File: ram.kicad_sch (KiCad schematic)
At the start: 7 parts, among them U1 LFE5U-25F-6BG381C, U2 MT48LC16M16A2TG

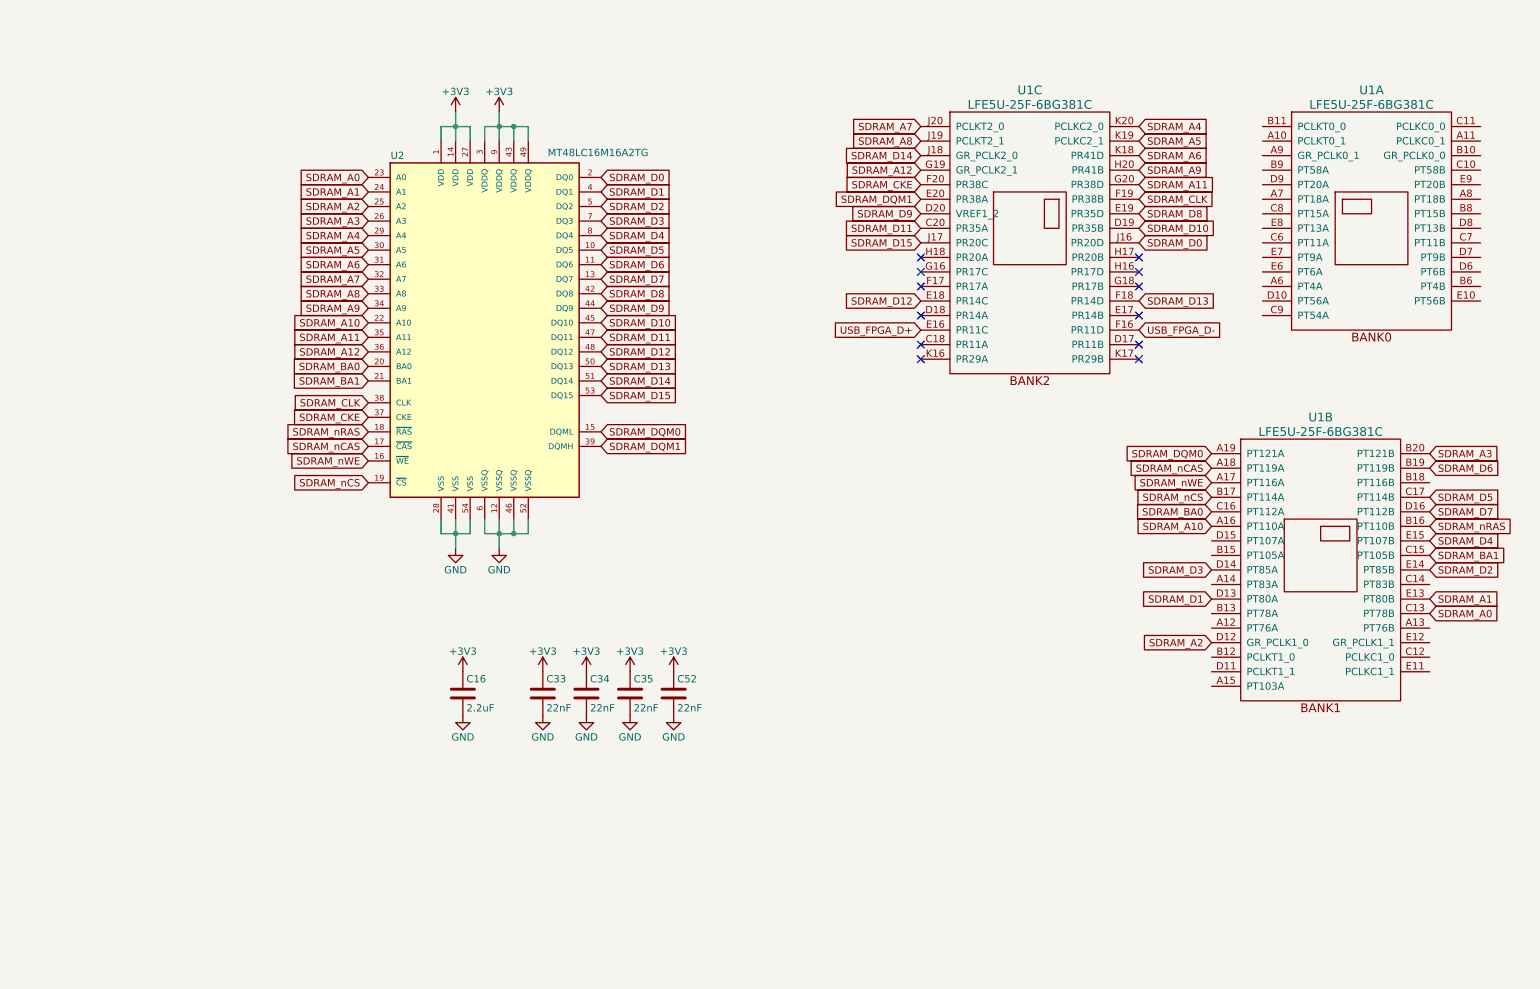
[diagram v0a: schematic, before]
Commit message: Routed Level Shifters + Flash
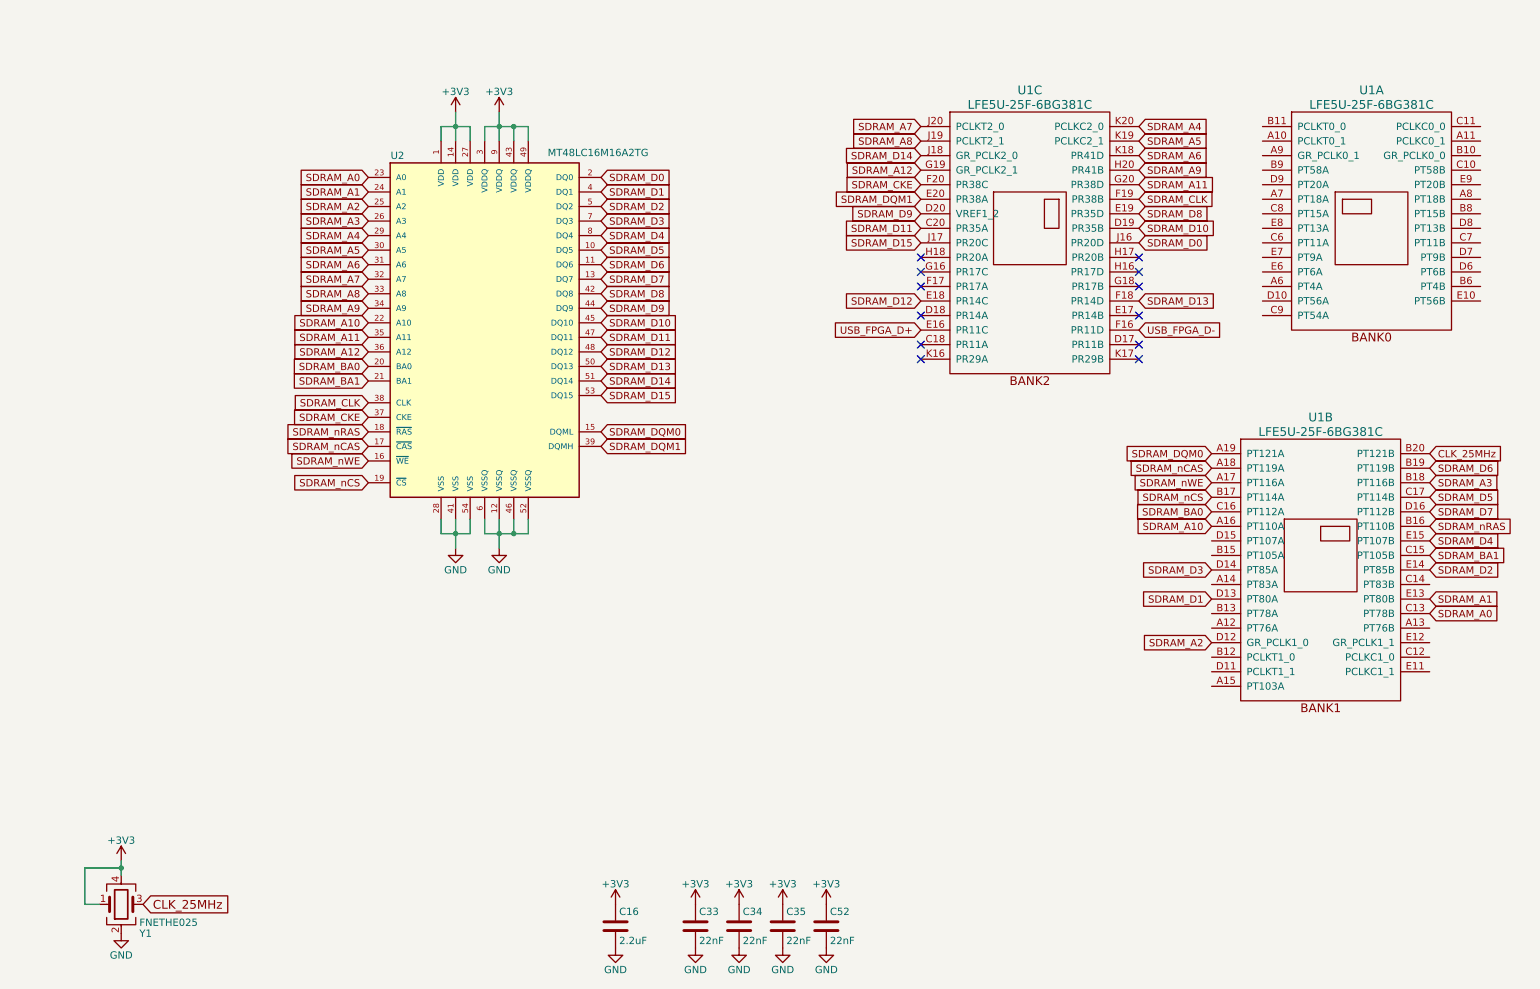
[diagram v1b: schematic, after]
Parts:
- added Y1: FNETHE025, oscxo:Crystal_SMD_7050_4Pads, symbol Device:Crystal_GND24
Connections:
- net +3V3: now also Y1.1, Y1.4
- net GND: now also Y1.2
- net SDRAM_A3: now also U1.B18 (PT116B); no longer U1.B20 (PT121B)
- new net CLK_25MHz: U1.B20 (PT121B), Y1.3
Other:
- moved on the sheet: C16, C33, C34, C35, C52

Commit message: Started SRAM routing
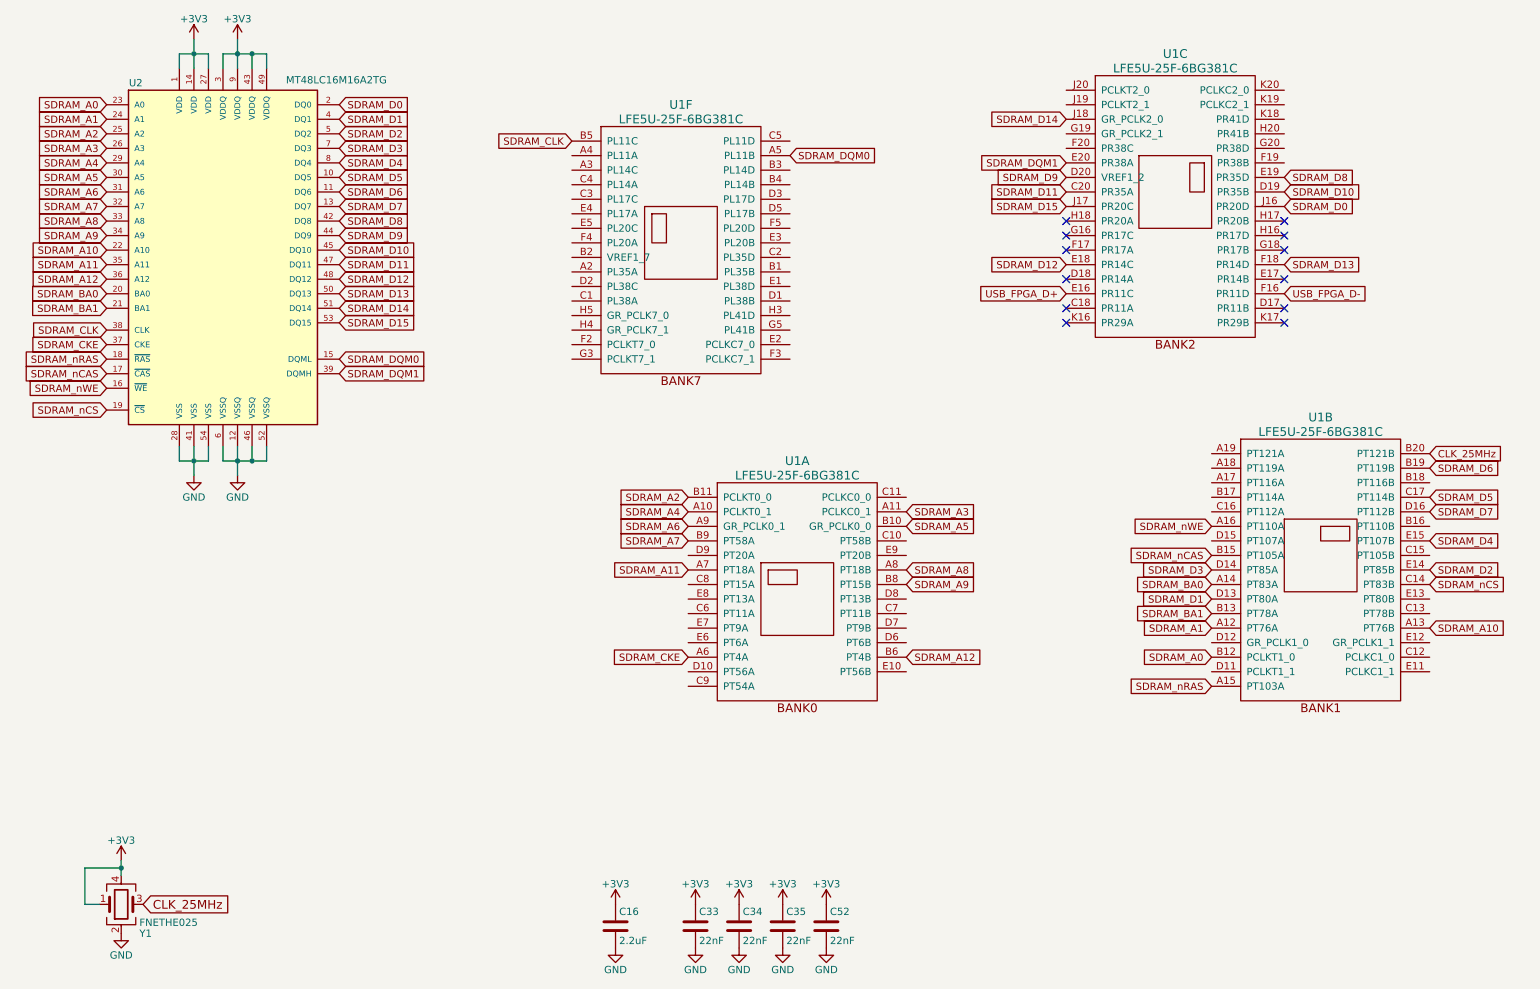
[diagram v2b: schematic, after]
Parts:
- added unit 6 of U1
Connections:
- net SDRAM_A0: now also U1.B12 (PCLKT1_0); no longer U1.C13 (PT78B)
- net SDRAM_A1: now also U1.A12 (PT76A); no longer U1.E13 (PT80B)
- net SDRAM_A10: now also U1.A13 (PT76B); no longer U1.A16 (PT110A)
- net SDRAM_A11: now also U1.A7 (PT18A); no longer U1.G20 (PR38D)
- net SDRAM_A12: now also U1.B6 (PT4B); no longer U1.G19 (GR_PCLK2_1)
- net SDRAM_A2: now also U1.B11 (PCLKT0_0); no longer U1.D12 (GR_PCLK1_0)
- net SDRAM_A3: now also U1.A11 (PCLKC0_1); no longer U1.B18 (PT116B)
- net SDRAM_A4: now also U1.A10 (PCLKT0_1); no longer U1.K20 (PCLKC2_0)
- net SDRAM_A5: now also U1.B10 (GR_PCLK0_0); no longer U1.K19 (PCLKC2_1)
- net SDRAM_A6: now also U1.A9 (GR_PCLK0_1); no longer U1.K18 (PR41D)
- net SDRAM_A7: now also U1.B9 (PT58A); no longer U1.J20 (PCLKT2_0)
- net SDRAM_A8: now also U1.A8 (PT18B); no longer U1.J19 (PCLKT2_1)
- net SDRAM_A9: now also U1.B8 (PT15B); no longer U1.H20 (PR41B)
- net SDRAM_BA0: now also U1.A14 (PT83A); no longer U1.C16 (PT112A)
- net SDRAM_BA1: now also U1.B13 (PT78A); no longer U1.C15 (PT105B)
- net SDRAM_CKE: now also U1.A6 (PT4A); no longer U1.F20 (PR38C)
- net SDRAM_CLK: now also U1.B5 (PL11C); no longer U1.F19 (PR38B)
- net SDRAM_DQM0: now also U1.A5 (PL11B); no longer U1.A19 (PT121A)
- net SDRAM_nCAS: now also U1.B15 (PT105A); no longer U1.A18 (PT119A)
- net SDRAM_nCS: now also U1.C14 (PT83B); no longer U1.B17 (PT114A)
- net SDRAM_nRAS: now also U1.A15 (PT103A); no longer U1.B16 (PT110B)
- net SDRAM_nWE: now also U1.A16 (PT110A); no longer U1.A17 (PT116A)
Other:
- moved on the sheet: U1A, U1C, U2

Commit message: Constraint Fixes
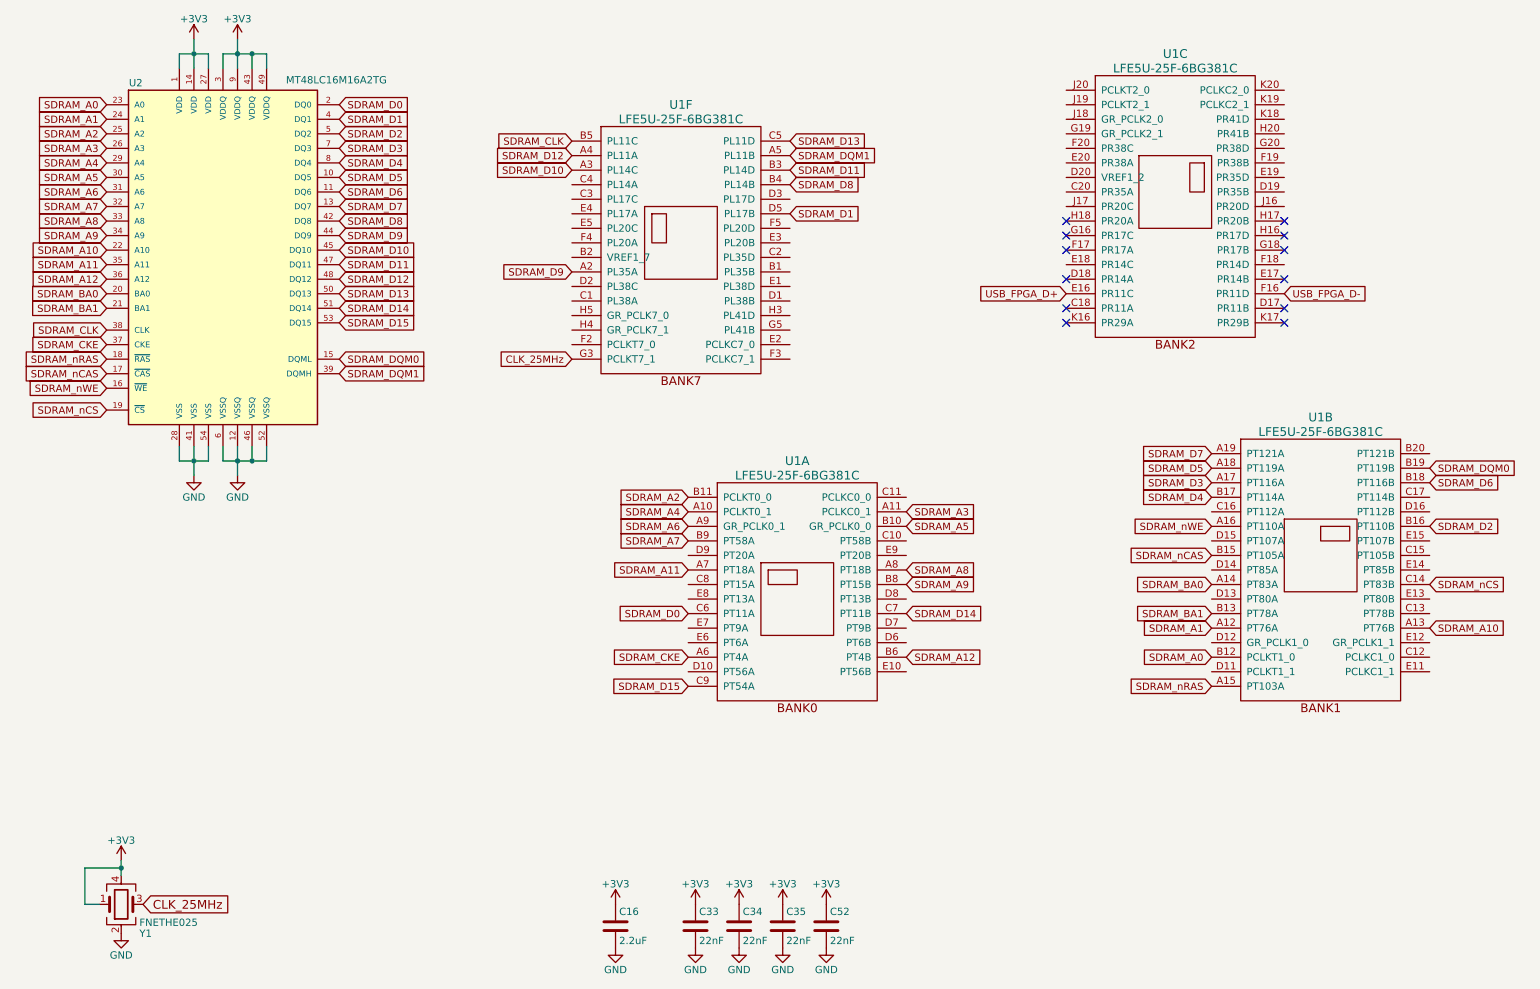
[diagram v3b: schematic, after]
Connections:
- net CLK_25MHz: now also U1.G3 (PCLKT7_1); no longer U1.B20 (PT121B)
- net SDRAM_D0: now also U1.C6 (PT11A); no longer U1.J16 (PR20D)
- net SDRAM_D1: now also U1.D5 (PL17B); no longer U1.D13 (PT80A)
- net SDRAM_D10: now also U1.A3 (PL14C); no longer U1.D19 (PR35B)
- net SDRAM_D11: now also U1.B3 (PL14D); no longer U1.C20 (PR35A)
- net SDRAM_D12: now also U1.A4 (PL11A); no longer U1.E18 (PR14C)
- net SDRAM_D13: now also U1.C5 (PL11D); no longer U1.F18 (PR14D)
- net SDRAM_D14: now also U1.C7 (PT11B); no longer U1.J18 (GR_PCLK2_0)
- net SDRAM_D15: now also U1.C9 (PT54A); no longer U1.J17 (PR20C)
- net SDRAM_D2: now also U1.B16 (PT110B); no longer U1.E14 (PT85B)
- net SDRAM_D3: now also U1.A17 (PT116A); no longer U1.D14 (PT85A)
- net SDRAM_D4: now also U1.B17 (PT114A); no longer U1.E15 (PT107B)
- net SDRAM_D5: now also U1.A18 (PT119A); no longer U1.C17 (PT114B)
- net SDRAM_D6: now also U1.B18 (PT116B); no longer U1.B19 (PT119B)
- net SDRAM_D7: now also U1.A19 (PT121A); no longer U1.D16 (PT112B)
- net SDRAM_D8: now also U1.B4 (PL14B); no longer U1.E19 (PR35D)
- net SDRAM_D9: now also U1.A2 (PL35A); no longer U1.D20 (VREF1_2)
- net SDRAM_DQM0: now also U1.B19 (PT119B); no longer U1.A5 (PL11B)
- net SDRAM_DQM1: now also U1.A5 (PL11B); no longer U1.E20 (PR38A)

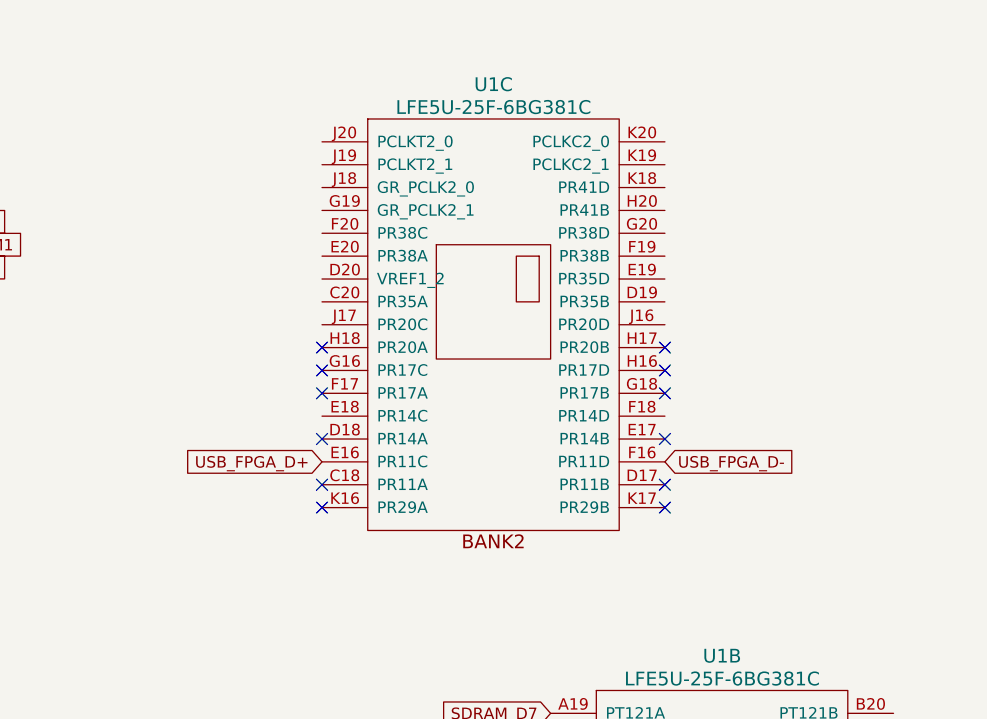
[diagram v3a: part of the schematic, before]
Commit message: Added Breakout pins + logo
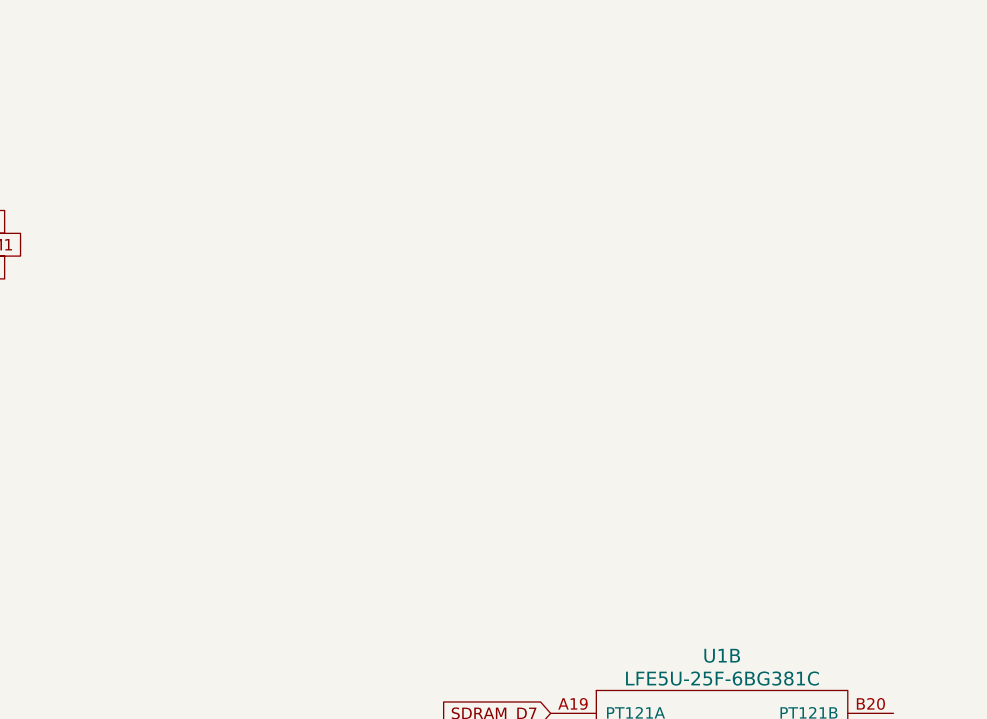
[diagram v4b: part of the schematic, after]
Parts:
- removed unit 3 of U1
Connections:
- no-connect marks 12 -> 0
